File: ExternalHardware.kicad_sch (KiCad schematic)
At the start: 17 parts, among them U6 74AHC04, U7 74AHC174, U8 74AHC08, U9 74AHC174

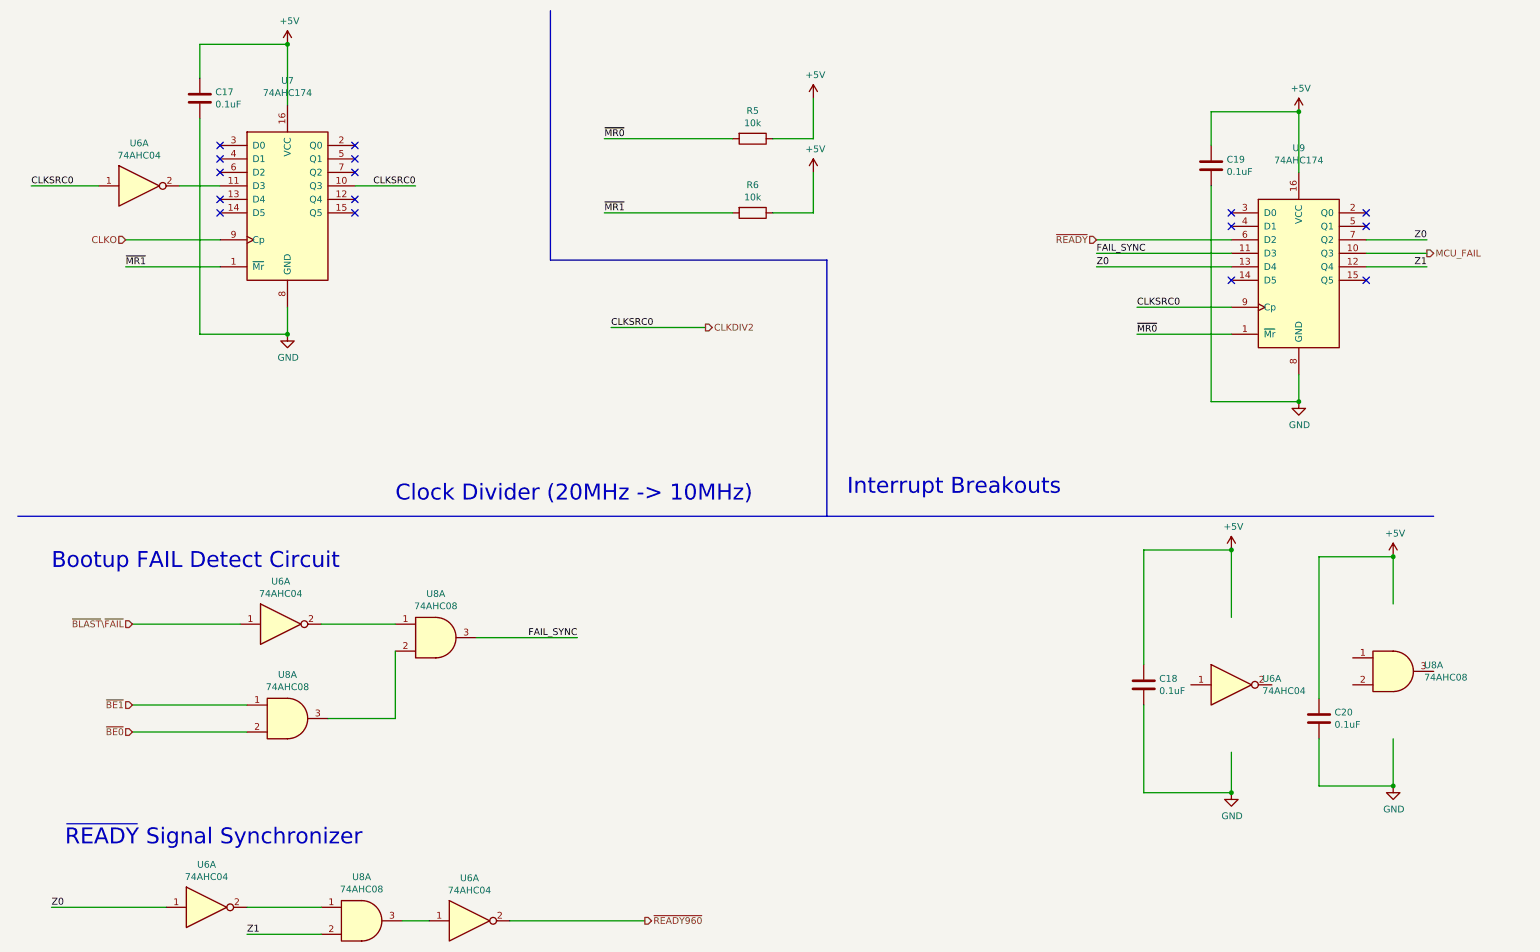
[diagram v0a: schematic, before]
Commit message: Use a GAL chip to consolidate the number of chips
I have many extra free entries on the GAL to assist me in doing stuff
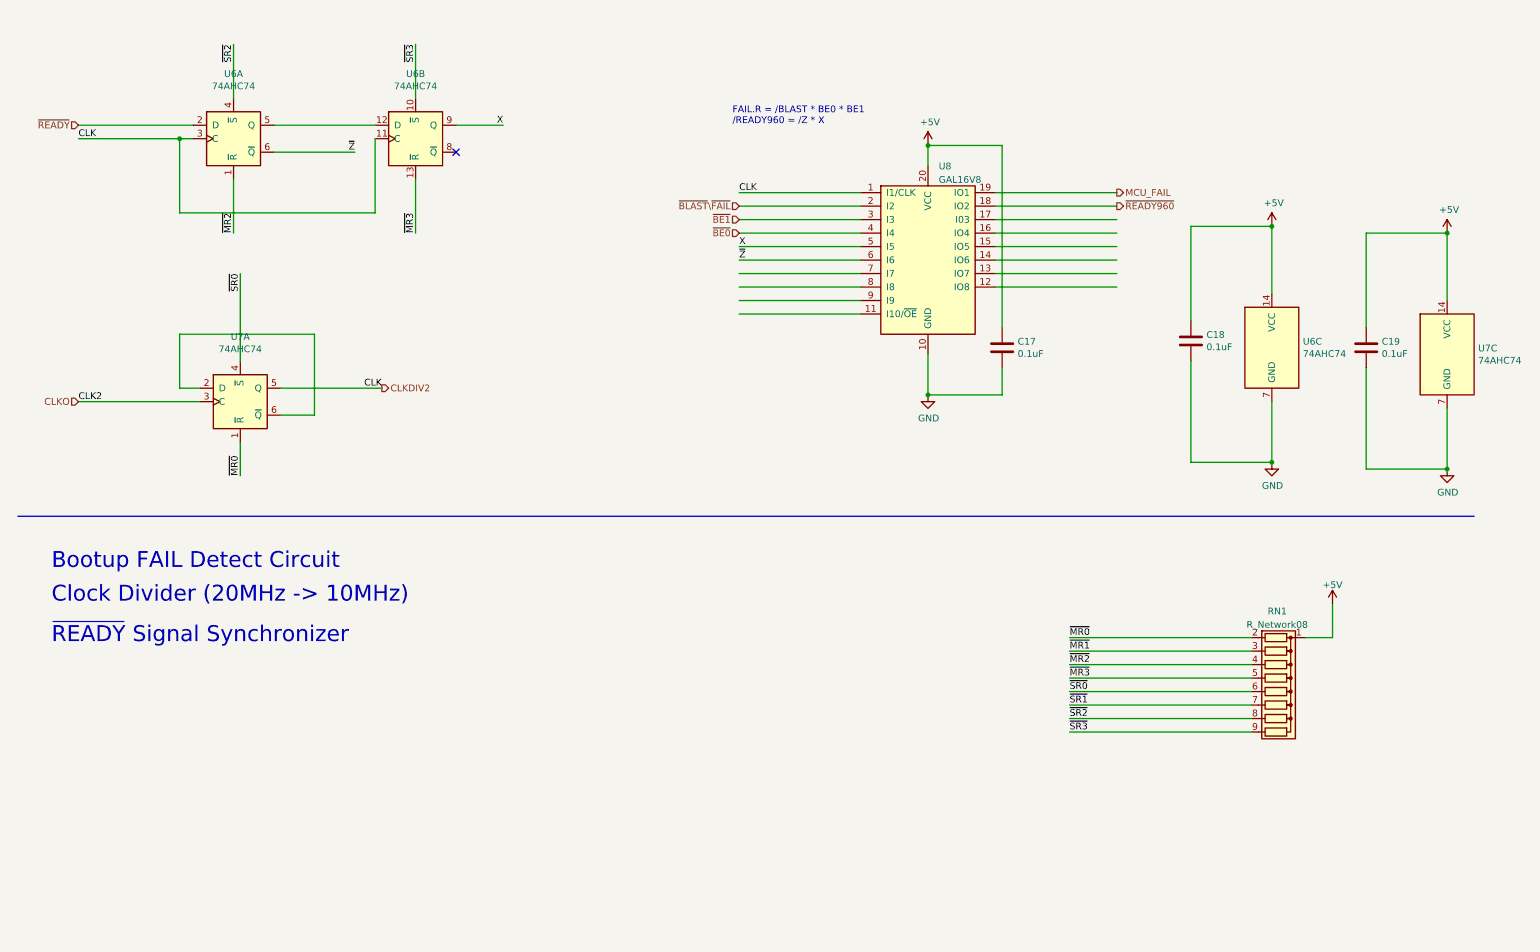
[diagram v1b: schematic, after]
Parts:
- removed C20: 0.1uF, Capacitor_SMD:C_0805_2012Metric_Pad1.18x1.45mm_HandSolder, symbol Device:C
- removed R5, R6: 10k, Resistor_SMD:R_0805_2012Metric_Pad1.20x1.40mm_HandSolder, symbol Device:R
- removed U6 (x5): 74AHC04, Package_SO:SOIC-14_3.9x8.7mm_P1.27mm, symbol 74xx:74LS04
- removed U7, U9: 74AHC174, Package_SO:SOIC-16_3.9x9.9mm_P1.27mm, symbol 74xx:74LS174
- removed U8 (x4): 74AHC08, Package_SO:SOIC-14_3.9x8.7mm_P1.27mm, symbol 74xx:74LS08
- added RN1: R_Network08, Resistor_THT:R_Array_SIP9, symbol Device:R_Network08
- added U6, U7: 74AHC74, Package_SO:SOIC-14_3.9x8.7mm_P1.27mm, symbol 74xx:74HC74
- added U8: GAL16V8, Package_DIP:DIP-20_W7.62mm_Socket, symbol Logic_Programmable:GAL16V8
- C18, C19: footprint Capacitor_SMD:C_0805_2012Metric_Pad1.18x1.45mm_HandSolder -> Capacitor_THT:C_Disc_D5.0mm_W2.5mm_P2.50mm
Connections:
- net +5V: now also RN1.1 (common), U6.14 (VCC), U7.14 (VCC), U8.20 (VCC)
- net CLKDIV2: now also U6.11 (C), U6.3 (C), U7.5 (Q), U8.1 (I1/CLK)
- net CLKO: now also U7.3 (C)
- net GND: now also U6.7 (GND), U7.7 (GND), U8.10 (GND)
- net MCU_FAIL: now also U8.19 (IO1)
- net ~{BE0}: now also U8.4 (I4)
- net ~{BE1}: now also U8.3 (I3)
- net ~{BLAST}\~{FAIL}: now also U8.2 (I2)
- net ~{MR0}: now also RN1.2 (R1), U7.1 (~{R})
- net ~{MR1}: now also RN1.3 (R2)
- net ~{READY960}: now also U8.18 (IO2)
- net ~{READY}: now also U6.2 (D)
- new net: U6.12 (D), U6.5 (Q)
- new net: U7.2 (D), U7.6 (~{Q})
- new net X: U6.9 (Q), U8.5 (I5)
- new net ~{MR2}: RN1.4 (R3), U6.1 (~{R})
- new net ~{MR3}: RN1.5 (R4), U6.13 (~{R})
- new net ~{SR0}: RN1.6 (R5), U7.4 (~{S})
- new net ~{SR1}: RN1.7 (R6)
- new net ~{SR2}: RN1.8 (R7), U6.4 (~{S})
- new net ~{SR3}: RN1.9 (R8), U6.10 (~{S})
- new net ~{Z}: U6.6 (~{Q}), U8.6 (I6)
- no-connect marks 16 -> 1
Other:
- note added: "FAIL.R = /BLAST * BE0 * BE1 /READY960 = /Z * X"
- note removed: "Interrupt Breakouts"
